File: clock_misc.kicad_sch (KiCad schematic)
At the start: 24 parts, among them J5 SWH, U19 74LVC1G06, U20 74LVC1G80, U21 FANOUT, Y1 TCXO

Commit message: Add footprints
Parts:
- J5: footprint (none) -> mainboard:Murata_SWH_MM8930-26xx
- U21: footprint (none) -> mainboard:Nexperia_XSON-8_1.95x1mm_P0.5mm
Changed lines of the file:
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@@
       (effects (font (size 1.27 1.27)) (justify left))
     )
-    (property "Footprint" "" (at 93.98 78.74 0)
+    (property "Footprint" "mainboard:Nexperia_XSON-8_1.95x1mm_P0.5mm" (at 93.98 78.74 0)
       (effects (font (size 1.27 1.27)) hide)
     )
@@
       (effects (font (size 1.27 1.27)))
     )
-    (property "Footprint" "" (at 76.2 76.2 0)
-      (effects (font (size 1.27 1.27)) hide)
-    )
+    (property "Footprint" "mainboard:Murata_SWH_MM8930-26xx" (at 76.2 76.2 0)
+      (effects (font (size 1.27 1.27)) hide)
+    )

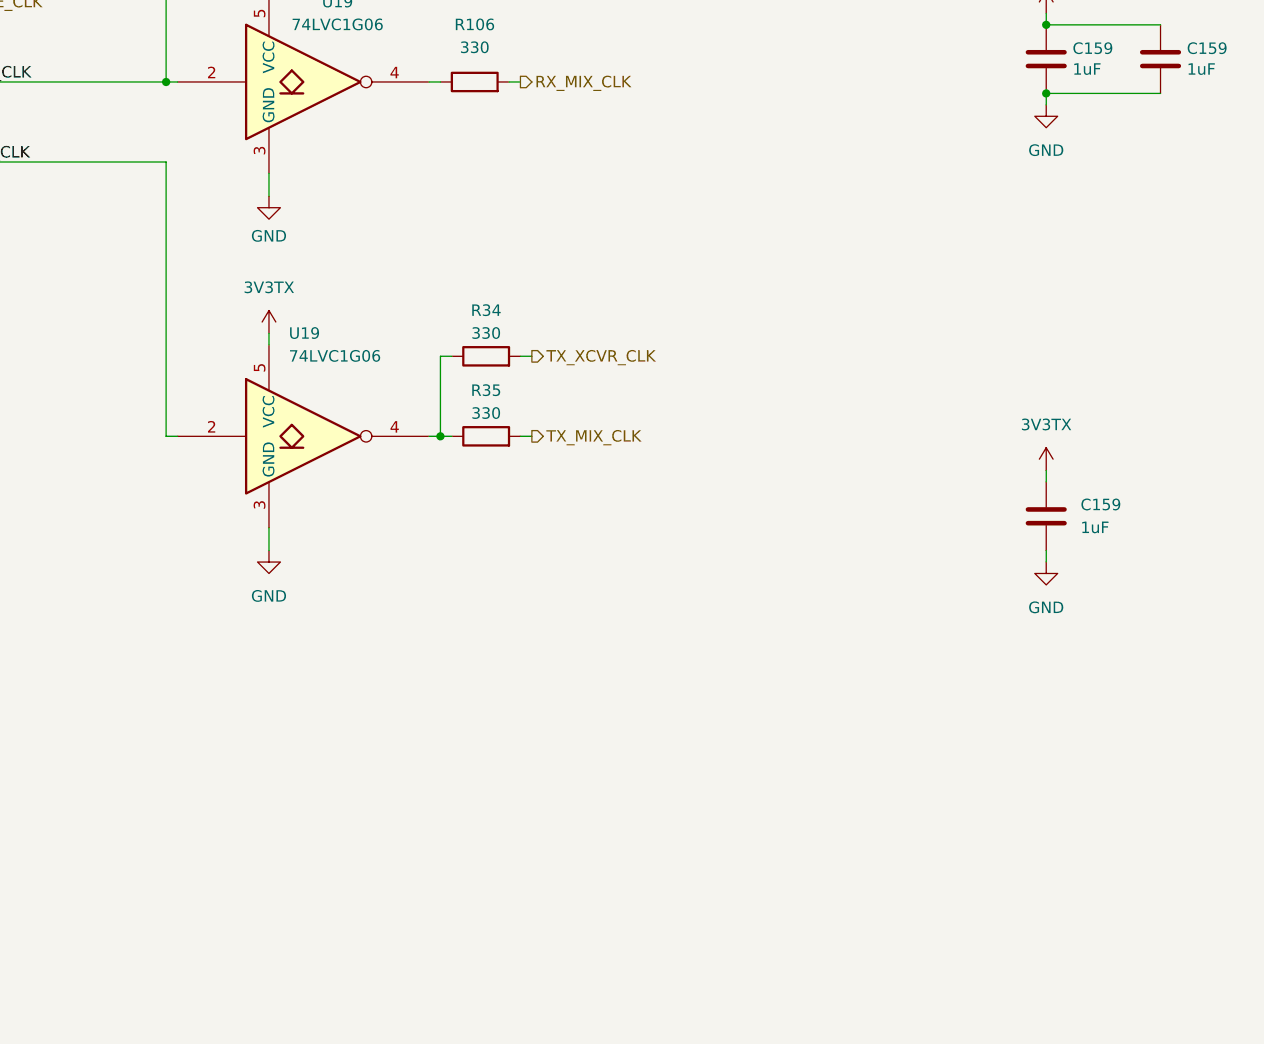
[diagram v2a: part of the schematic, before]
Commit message: layout wip: radio FPGA connections and clocks
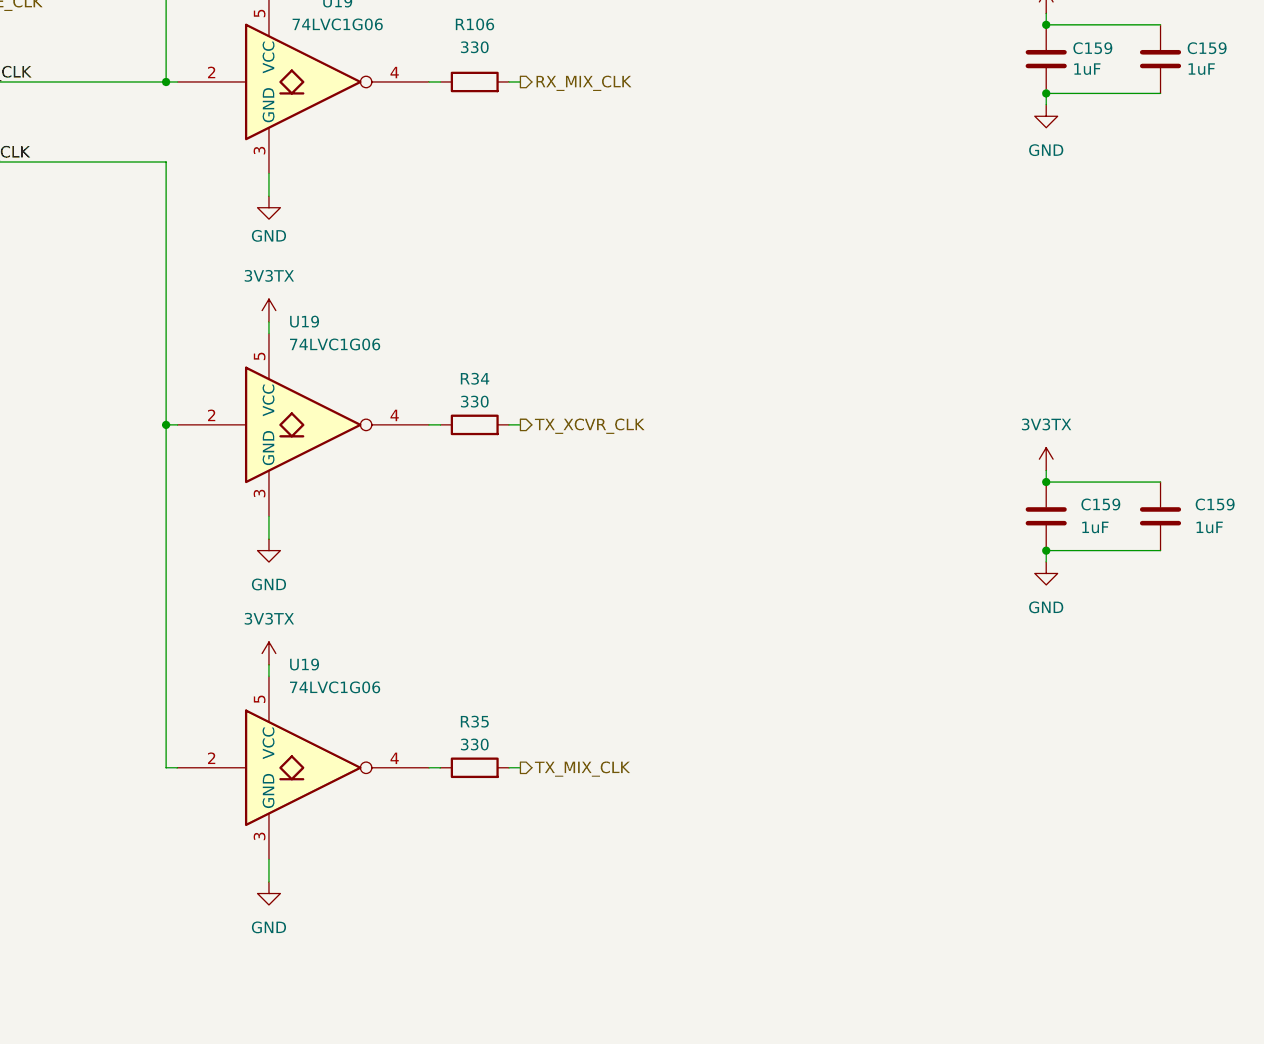
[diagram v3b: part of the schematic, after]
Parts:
- added C159: 1uF, Capacitor_SMD:C_0402_1005Metric, symbol Device:C
- added U19: 74LVC1G06, Package_TO_SOT_SMD:SOT-353_SC-70-5, symbol 74xGxx:74LVC1G06
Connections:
- net 3V3TX: now also C159.1, U19.5 (VCC)
- net GND: now also C159.2, U19.3 (GND)
- net TX_CLK: now also U19.2
- net at R34.1, U19.4: no longer R35.1
- new net: R35.1, U19.4
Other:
- moved on the sheet: R34, R35, U19

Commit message: more layout wip
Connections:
- net at R105.1: now also U21.6 (Y2); no longer U21.5 (Y1)
- net at R104.1: now also U21.5 (Y1); no longer U21.6 (Y2)
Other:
- moved on the sheet: C159, C39, J5, R103, R104, R105, R106, R34, R35, R36, R45, TP34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

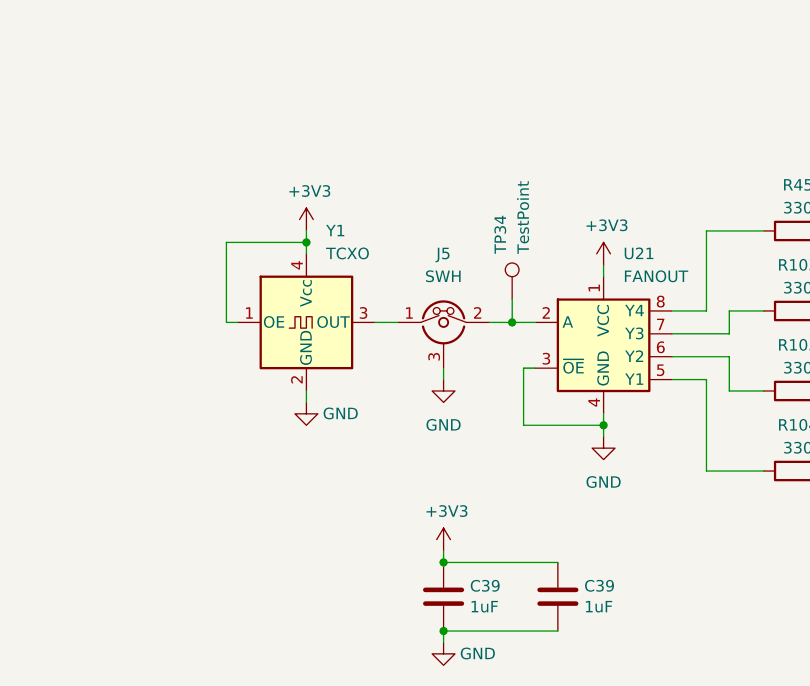
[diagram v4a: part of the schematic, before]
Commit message: complete initial layout
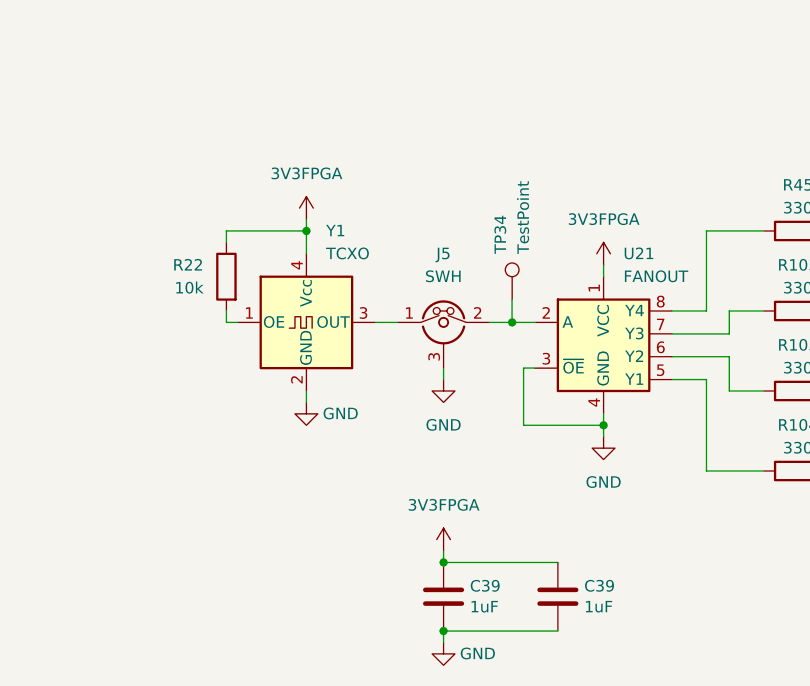
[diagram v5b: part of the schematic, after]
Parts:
- added R22: 10k, Resistor_SMD:R_0402_1005Metric, symbol Device:R
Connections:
- net +3V3 renamed 3V3FPGA
- net 3V3FPGA: now also R22.1; no longer Y1.1 (OE)
- new net: R22.2, Y1.1 (OE)
